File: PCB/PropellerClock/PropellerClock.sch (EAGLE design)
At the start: 32 parts

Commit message: 基板第一弾完成
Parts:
- removed IC2: (no value), v-reg:78XXL
- added C4: (no value), rcl:C-EUC2012
- U$2: value CR2032-HOLDER -> CR2032-HOLDER2; device CR2032-holder:CR2032-HOLDER -> CR2032-holder:CR2032-HOLDER2
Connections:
- removed net 3VR: IC1.VDD, U$2.3VR
- removed net N$1: C2.1, C3.1, IC2.IN, PAD2.P
- new net N$4: IC1.VDD, U$2.+3V
- net +3V3: now also C2.1, C3.1, C4.1, PAD2.P; no longer IC2.OUT
- net GND: now also C4.2; no longer IC2.GND
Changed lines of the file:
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@@
 <part name="LED9" library="led" deviceset="LED" device="3MM"/>
 <part name="LED10" library="led" deviceset="LED" device="3MM"/>
-<part name="IC2" library="v-reg" deviceset="78XXL" device=""/>
 <part name="C1" library="rcl" deviceset="C-EU" device="C3216"/>
 <part name="C2" library="rcl" deviceset="C-EU" device="C3216"/>
@@
 <part name="XT1" library="serolock" deviceset="CERALOCK" device=""/>
 <part name="GND2" library="supply1" deviceset="GND" device=""/>
-<part name="U$2" library="CR2032-holder" deviceset="CR2032-HOLDER" device=""/>
 <part name="GND4" library="supply1" deviceset="GND" device=""/>
 <part name="GND5" library="supply1" deviceset="GND" device=""/>
@@
 <part name="R12" library="rcl" deviceset="R-US_" device="0207/7"/>
 <part name="GND6" library="supply1" deviceset="GND" device=""/>
+<part name="U$2" library="CR2032-holder" deviceset="CR2032-HOLDER2" device=""/>
+<part name="C4" library="rcl" deviceset="C-EU" device="C2012"/>
 </parts>
 <sheets>
@@
 <instance part="LED9" gate="G$1" x="355.6" y="0"/>
 <instance part="LED10" gate="G$1" x="363.22" y="0"/>
-<instance part="IC2" gate="A" x="193.04" y="121.92"/>
 <instance part="C1" gate="G$1" x="208.28" y="119.38"/>
 <instance part="C2" gate="G$1" x="175.26" y="119.38"/>
@@
 <instance part="XT1" gate="G$1" x="205.74" y="71.12" rot="R180"/>
 <instance part="GND2" gate="1" x="205.74" y="60.96"/>
-<instance part="U$2" gate="G$1" x="149.86" y="91.44"/>
 <instance part="GND4" gate="1" x="154.94" y="83.82"/>
 <instance part="GND5" gate="1" x="99.06" y="78.74"/>
@@
 <instance part="R12" gate="G$1" x="363.22" y="-10.16" rot="R270"/>
 <instance part="GND6" gate="1" x="266.7" y="-22.86"/>
+<instance part="U$2" gate="G$1" x="144.78" y="93.98"/>
+<instance part="C4" gate="G$1" x="152.4" y="119.38"/>
 </instances>
 <busses>
@@
 </busses>
 <nets>
-<net name="N$1" class="0">
-<segment>
-<pinref part="IC2" gate="A" pin="IN"/>
-<pinref part="C3" gate="G$1" pin="1"/>
-<wire x1="185.42" y1="121.92" x2="175.26" y2="121.92" width="0.1524" layer="91"/>
-<pinref part="C2" gate="G$1" pin="1"/>
-<wire x1="175.26" y1="121.92" x2="165.1" y2="121.92" width="0.1524" layer="91"/>
-<junction x="175.26" y="121.92"/>
-<pinref part="PAD2" gate="P" pin="P"/>
-<wire x1="165.1" y1="129.54" x2="165.1" y2="121.92" width="0.1524" layer="91"/>
-</segment>
-</net>
 <net name="GND" class="0">
 <segment>
 <pinref part="C3" gate="G$1" pin="2"/>
-<pinref part="IC2" gate="A" pin="GND"/>
 <wire x1="165.1" y1="114.3" x2="175.26" y2="114.3" width="0.1524" layer="91"/>
 <pinref part="GND1" gate="1" pin="GND"/>
@@
 <pinref part="PAD1" gate="P" pin="P"/>
 <wire x1="208.28" y1="114.3" x2="208.28" y2="109.22" width="0.1524" layer="91"/>
+<pinref part="C4" gate="G$1" pin="2"/>
+<wire x1="152.4" y1="114.3" x2="165.1" y2="114.3" width="0.1524" layer="91"/>
 </segment>
 <segment>
@@
 </segment>
 <segment>
+<pinref part="GND4" gate="1" pin="GND"/>
+<wire x1="154.94" y1="93.98" x2="154.94" y2="86.36" width="0.1524" layer="91"/>
 <pinref part="U$2" gate="G$1" pin="GND"/>
-<pinref part="GND4" gate="1" pin="GND"/>
-<wire x1="154.94" y1="91.44" x2="154.94" y2="86.36" width="0.1524" layer="91"/>
+<wire x1="152.4" y1="93.98" x2="154.94" y2="93.98" width="0.1524" layer="91"/>
 </segment>
 <segment>
@@
 <net name="+3V3" class="0">
 <segment>
-<pinref part="IC2" gate="A" pin="OUT"/>
 <pinref part="C1" gate="G$1" pin="1"/>
-<wire x1="200.66" y1="121.92" x2="208.28" y2="121.92" width="0.1524" layer="91"/>
 <pinref part="+3V1" gate="G$1" pin="+3V3"/>
 <wire x1="208.28" y1="121.92" x2="208.28" y2="132.08" width="0.1524" layer="91"/>
+<pinref part="C3" gate="G$1" pin="1"/>
+<pinref part="C2" gate="G$1" pin="1"/>
+<wire x1="175.26" y1="121.92" x2="165.1" y2="121.92" width="0.1524" layer="91"/>
+<junction x="175.26" y="121.92"/>
+<pinref part="PAD2" gate="P" pin="P"/>
+<wire x1="165.1" y1="129.54" x2="165.1" y2="121.92" width="0.1524" layer="91"/>
+<wire x1="175.26" y1="121.92" x2="208.28" y2="121.92" width="0.1524" layer="91"/>
+<pinref part="C4" gate="G$1" pin="1"/>
+<wire x1="165.1" y1="121.92" x2="152.4" y2="121.92" width="0.1524" layer="91"/>
 </segment>
 <segment>
@@
 <pinref part="U$1" gate="A" pin="RA4/AN3/*T1G/OSC2/CLKOUT"/>
 <wire x1="213.36" y1="73.66" x2="231.14" y2="73.66" width="0.1524" layer="91"/>
-</segment>
-</net>
-<net name="3VR" class="0">
-<segment>
-<pinref part="U$2" gate="G$1" pin="3VR"/>
-<pinref part="IC1" gate="G$1" pin="VDD"/>
-<wire x1="137.16" y1="93.98" x2="127" y2="93.98" width="0.1524" layer="91"/>
-<wire x1="127" y1="93.98" x2="127" y2="88.9" width="0.1524" layer="91"/>
 </segment>
 </net>
@@
 </segment>
 </net>
+<net name="N$4" class="0">
+<segment>
+<pinref part="IC1" gate="G$1" pin="VDD"/>
+<wire x1="137.16" y1="93.98" x2="127" y2="93.98" width="0.1524" layer="91"/>
+<wire x1="127" y1="93.98" x2="127" y2="88.9" width="0.1524" layer="91"/>
+<pinref part="U$2" gate="G$1" pin="+3V"/>
+</segment>
+</net>

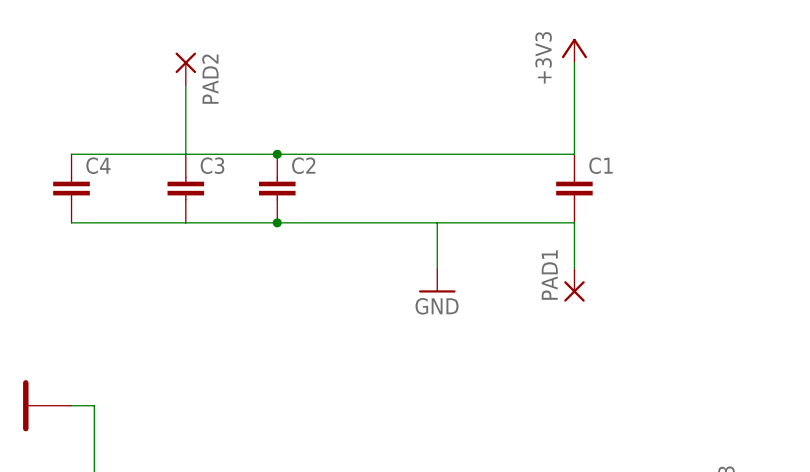
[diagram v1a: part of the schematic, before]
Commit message: プロペラ部の回路を作成
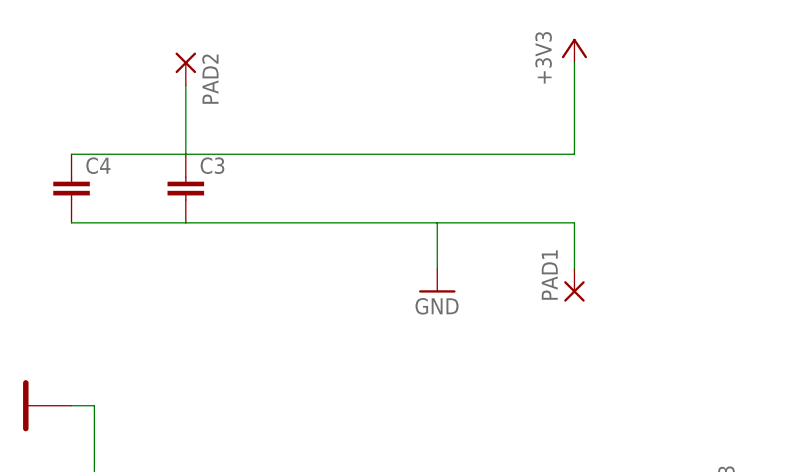
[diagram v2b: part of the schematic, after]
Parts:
- removed C1, C2: (no value), rcl:C-EUC3216
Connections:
- net +3V3: no longer C1.1, C2.1
- net GND: no longer C1.2, C2.2
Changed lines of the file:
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@@
 <setting verticaltext="up"/>
 </settings>
-<grid distance="0.1" unitdist="inch" unit="inch" style="lines" multiple="1" display="no" altdistance="0.01" altunitdist="inch" altunit="inch"/>
+<grid distance="0.1" unitdist="inch" unit="mm" style="lines" multiple="1" display="no" altdistance="0.01" altunitdist="inch" altunit="inch"/>
 <layers>
 <layer number="1" name="Top" color="4" fill="1" visible="no" active="no"/>
@@
 <class number="0" name="default" width="0" drill="0">
 </class>
+<class number="1" name="power" width="1" drill="0">
+</class>
+<class number="2" name="GND" width="1" drill="0">
+</class>
 </classes>
 <parts>
@@
 <part name="LED9" library="led" deviceset="LED" device="3MM"/>
 <part name="LED10" library="led" deviceset="LED" device="3MM"/>
-<part name="C1" library="rcl" deviceset="C-EU" device="C3216"/>
-<part name="C2" library="rcl" deviceset="C-EU" device="C3216"/>
 <part name="C3" library="rcl" deviceset="C-EU" device="C2012"/>
 <part name="GND1" library="supply1" deviceset="GND" device=""/>
@@
 <instance part="LED9" gate="G$1" x="355.6" y="0"/>
 <instance part="LED10" gate="G$1" x="363.22" y="0"/>
-<instance part="C1" gate="G$1" x="208.28" y="119.38"/>
-<instance part="C2" gate="G$1" x="175.26" y="119.38"/>
 <instance part="C3" gate="G$1" x="165.1" y="119.38"/>
 <instance part="GND1" gate="1" x="193.04" y="106.68"/>
@@
 </busses>
 <nets>
-<net name="GND" class="0">
-<segment>
-<pinref part="C3" gate="G$1" pin="2"/>
-<wire x1="165.1" y1="114.3" x2="175.26" y2="114.3" width="0.1524" layer="91"/>
+<net name="GND" class="2">
+<segment>
 <pinref part="GND1" gate="1" pin="GND"/>
-<wire x1="175.26" y1="114.3" x2="193.04" y2="114.3" width="0.1524" layer="91"/>
 <wire x1="193.04" y1="114.3" x2="193.04" y2="109.22" width="0.1524" layer="91"/>
-<pinref part="C1" gate="G$1" pin="2"/>
 <wire x1="208.28" y1="114.3" x2="193.04" y2="114.3" width="0.1524" layer="91"/>
-<pinref part="C2" gate="G$1" pin="2"/>
-<junction x="175.26" y="114.3"/>
 <pinref part="PAD1" gate="P" pin="P"/>
 <wire x1="208.28" y1="114.3" x2="208.28" y2="109.22" width="0.1524" layer="91"/>
+<pinref part="C3" gate="G$1" pin="2"/>
 <pinref part="C4" gate="G$1" pin="2"/>
 <wire x1="152.4" y1="114.3" x2="165.1" y2="114.3" width="0.1524" layer="91"/>
+<wire x1="165.1" y1="114.3" x2="193.04" y2="114.3" width="0.1524" layer="91"/>
 </segment>
 <segment>
@@
 </segment>
 </net>
-<net name="+3V3" class="0">
-<segment>
-<pinref part="C1" gate="G$1" pin="1"/>
+<net name="+3V3" class="1">
+<segment>
 <pinref part="+3V1" gate="G$1" pin="+3V3"/>
 <wire x1="208.28" y1="121.92" x2="208.28" y2="132.08" width="0.1524" layer="91"/>
 <pinref part="C3" gate="G$1" pin="1"/>
-<pinref part="C2" gate="G$1" pin="1"/>
-<wire x1="175.26" y1="121.92" x2="165.1" y2="121.92" width="0.1524" layer="91"/>
-<junction x="175.26" y="121.92"/>
 <pinref part="PAD2" gate="P" pin="P"/>
 <wire x1="165.1" y1="129.54" x2="165.1" y2="121.92" width="0.1524" layer="91"/>
-<wire x1="175.26" y1="121.92" x2="208.28" y2="121.92" width="0.1524" layer="91"/>
+<wire x1="165.1" y1="121.92" x2="208.28" y2="121.92" width="0.1524" layer="91"/>
 <pinref part="C4" gate="G$1" pin="1"/>
 <wire x1="165.1" y1="121.92" x2="152.4" y2="121.92" width="0.1524" layer="91"/>
@@
 </segment>
 </net>
-<net name="N$4" class="0">
+<net name="N$4" class="1">
 <segment>
 <pinref part="IC1" gate="G$1" pin="VDD"/>
